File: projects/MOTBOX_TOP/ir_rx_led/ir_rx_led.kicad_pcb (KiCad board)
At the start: 2 copper layers, 8 x 8 mm, 2 parts, among them J1 Conn_01x02

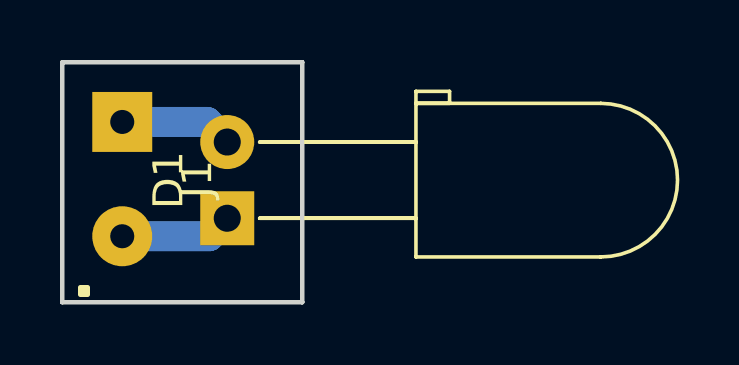
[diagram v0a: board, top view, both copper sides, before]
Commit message: New library files and schematics with ESE31 and DT045 switches
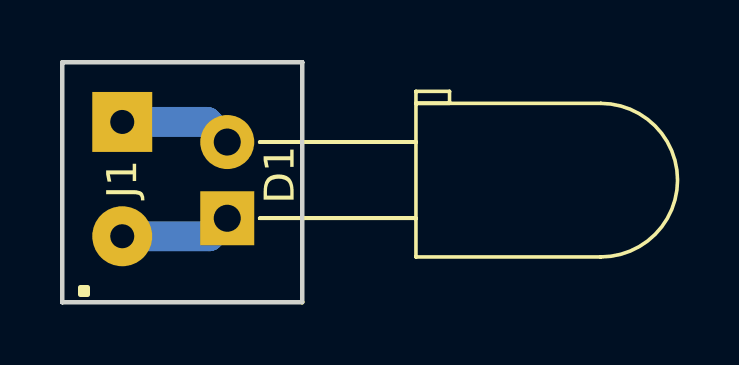
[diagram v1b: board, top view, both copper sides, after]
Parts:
- D1: value D_Photo -> PD333-3B/H0/L2
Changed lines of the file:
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@@
     (solder_mask_min_width 0.25)
     (aux_axis_origin 0 0)
-    (visible_elements FFF9FF7F)
+    (visible_elements FFFDFF7F)
     (pcbplotparams
-      (layerselection 0x010fc_ffffffff)
-      (usegerberextensions false)
+      (layerselection 0x010fc_fffffffe)
+      (usegerberextensions true)
       (usegerberattributes false)
       (usegerberadvancedattributes false)
@@
       (outputformat 1)
       (mirror false)
-      (drillshape 1)
+      (drillshape 0)
       (scaleselection 1)
-      (outputdirectory ""))
+      (outputdirectory "Gerber/"))
   )
   (net 0 "")
@@
     (descr "LED, diameter 5.0mm z-position of LED center 3.0mm, 2 pins, diameter 5.0mm z-position of LED center 3.0mm, 2 pins, diameter 5.0mm z-position of LED center 3.0mm, 2 pins, diameter 5.0mm z-position of LED center 9.0mm, 2 pins, diameter 5.0mm z-position of LED center 9.0mm, 2 pins, diameter 5.0mm z-position of LED center 9.0mm, 2 pins")
     (tags "LED diameter 5.0mm z-position of LED center 3.0mm 2 pins diameter 5.0mm z-position of LED center 3.0mm 2 pins diameter 5.0mm z-position of LED center 3.0mm 2 pins diameter 5.0mm z-position of LED center 9.0mm 2 pins diameter 5.0mm z-position of LED center 9.0mm 2 pins diameter 5.0mm z-position of LED center 9.0mm 2 pins")
-    (fp_text reference D1 (at 1.27 -1.96 90) (layer F.SilkS)
+    (fp_text reference D1 (at 1.45 1.75 90) (layer F.SilkS)
       (effects (font (size 1 1) (thickness 0.15)))
     )
-    (fp_text value D_Photo (at 1.27 16.01 90) (layer F.Fab)
+    (fp_text value PD333-3B/H0/L2 (at 1.27 16.01 90) (layer F.Fab)
       (effects (font (size 1 1) (thickness 0.15)))
     )
@@
     (tags connector)
     (attr virtual)
-    (fp_text reference J1 (at 1.905 -2.5 270) (layer F.SilkS)
+    (fp_text reference J1 (at 1.905 0 270) (layer F.SilkS)
       (effects (font (size 1 1) (thickness 0.15)))
     )
@@
       (net 1 "Net-(D1-Pad1)"))
   )
+  (gr_poly (pts (xy 107.6 93.5) (xy 107.85 93.5) (xy 107.85 93.75) (xy 107.6 93.75)) (layer F.SilkS) (width 0.15))
   (gr_line (start 115 86) (end 107 86) (layer Edge.Cuts) (width 0.15))
   (gr_line (start 115 94) (end 115 86) (layer Edge.Cuts) (width 0.15))
   (gr_line (start 107 94) (end 115 94) (layer Edge.Cuts) (width 0.15))
   (gr_line (start 107 86) (end 107 94) (layer Edge.Cuts) (width 0.15))
-  (gr_poly (pts (xy 107.6 93.5) (xy 107.85 93.5) (xy 107.85 93.75) (xy 107.6 93.75)) (layer F.SilkS) (width 0.15))
   (segment (start 111.8 91.55) (end 112.05 91.3) (width 0.25) (layer B.Cu) (net 1))
   (segment (start 111.9 91.8) (end 112.5 91.2) (width 1) (layer B.Cu) (net 1))
